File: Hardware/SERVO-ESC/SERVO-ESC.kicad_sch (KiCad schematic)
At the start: 43 parts, among them IC1 DRV8876PWPR, IC2 TMP102xxDRL, IC3 INA236AIDDFR, IC4 MT6816CT, IC5 AP2112K, J1 Conn_01x04_Pin, J2 Conn_01x04_Pin, J3 Conn_01x05_Pin, J4 Conn_01x05, J5 +, J6 -, U1 STM32F301C8Tx, Y1 25MHZ

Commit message: New PCB Files
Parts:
- removed C13: 100nF, Capacitor_SMD:C_0402_1005Metric, symbol Device:C
- removed C14, C16: 10nF, Capacitor_SMD:C_0402_1005Metric, symbol Device:C
- removed D1: 6V, Diode_SMD:D_0402_1005Metric, symbol Device:D
- removed FB1: 120, Inductor_SMD:L_0603_1608Metric, symbol Device:FerriteBead
- removed IC4: MT6816CT, Package_SO:SO-8_3.9x4.9mm_P1.27mm, symbol Sensor_Magnetic:MT6816CT
- removed J3: Conn_01x05_Pin, Connector_JST:JST_SH_SM05B-SRSS-TB_1x05-1MP_P1.00mm_Horizontal, symbol Connector:Conn_01x05_Pin
- added D1: LED, LED_SMD:LED_0603_1608Metric, symbol Device:LED
- added R1: 10k, Resistor_SMD:R_0402_1005Metric, symbol Device:R
- added R12, R13: 4.7k, Resistor_SMD:R_0402_1005Metric, symbol Device:R
- added R7: 1k, Resistor_SMD:R_0402_1005Metric, symbol Device:R
- J4: footprint Connector_PinSocket_1.00mm:PinSocket_1x05_P1.00mm_Vertical -> Connector_PinHeader_2.00mm:PinHeader_1x05_P2.00mm_Vertical
- renumbered C7 to C1, C3 to C10, C4 to C11, C15 to C12, C5 to C13, C6 to C14, C12 to C15, C8 to C2, C9 to C3, C10 to C4, C11 to C5, C17 to C6, C1 to C7, C18 to C8, C2 to C9, IC5 to IC1, IC1 to IC2, IC2 to IC4, IC3 to IC5, R2 to R10, R1 to R11, R7 to R2, R6 to R3, R5 to R4, R8 to R5, R9 to R6, R3 to R8, R4 to R9
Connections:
- net +3.3VA is gone; now on net +3.3V: C12.1, U1.9 (VDDA)
- net 3.3V is gone; now on net +3.3V: J2.4 (Pin_4)
- net +3.3V: now also D1.2 (A), R12.1, R13.1
- net GND: now also R1.1, R7.2
- net I2C-SCL-1: now also R5.2; no longer R6.2
- net I2C-SDA-1: now also R6.2, U1.43 (PB7); no longer R5.2, U1.41 (PB5)
- net INA236-INT: now also U1.45 (PB8), R12.2
- net MAG-MOSI: now also U1.28 (PB15); no longer U1.26 (PB13)
- net MAG-SCLK: now also U1.26 (PB13); no longer U1.28 (PB15)
- net TMP102-INT: now also R13.2
- net at U1.44 (BOOT0): now also R1.2
- net I2C-SCL-2 renamed UART-TX
- net I2C-SDA-2 renamed UART-RX
- new net: D1.1 (K), R7.1
- no-connect marks 2 -> 16
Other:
- moved on the sheet: C12, J4

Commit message: New Commit
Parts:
- removed J4: Conn_01x05, Connector_PinHeader_2.00mm:PinHeader_1x05_P2.00mm_Vertical, symbol Connector_Generic:Conn_01x05
- added C16: 10nF, Capacitor_SMD:C_0402_1005Metric, symbol Device:C
- added D2: TVS 6V, Diode_SMD:D_0402_1005Metric, symbol Diode:SMF6V0A
- added J3: MAG, Connector_PinSocket_2.00mm:PinSocket_1x04_P2.00mm_Vertical, symbol Connector:Conn_01x04_Pin
- added J4: Conn_01x04_Pin, Connector_PinSocket_2.54mm:PinSocket_1x04_P2.54mm_Vertical, symbol Connector:Conn_01x04_Pin
- added R14, R15: 4.7k, Resistor_SMD:R_0402_1005Metric, symbol Device:R
- added U2: MT6701CT, Package_SO:SO-8_3.9x4.9mm_P1.27mm, symbol Sensor_Magnetic:MT6701CT
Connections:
- net MAG-MISO is gone; now on net HBRIDGE-IN2: U1.27 (PB14)
- net MAG-MOSI is gone; now on net HBRIDGE-IN1: U1.28 (PB15)
- net +3.3V: now also R8.2, C16.1, D2.1 (A1), J3.4 (Pin_4), J4.4 (Pin_4), R14.1, R15.1, U2.1 (VDD), U2.2 (MODE), U2.8 (Z)
- net GND: now also C16.2, D2.2 (A2), J3.1 (Pin_1), J4.3 (Pin_3), U2.4 (GND); no longer R8.2
- net HBRIDGE-IN1: no longer U1.32 (PA11)
- net HBRIDGE-IN2: no longer U1.29 (PA8)
- net I2C-SDA-3: now reaches U1.41 (PB5)
- net I2C-SDA-3: now also J3.3 (Pin_3), J4.1 (Pin_1), R15.2, U2.6 (A)
- net MAG-SCLK: no longer names the net of U1.26 (PB13)
- new net I2C-SCL-3: J3.2 (Pin_2), J4.2 (Pin_2), R14.2, U1.29 (PA8), U2.7 (B)
- no-connect marks 16 -> 19
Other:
- moved on the sheet: C12, C15, R5, R6, R8

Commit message: New stuff
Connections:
- net +3.3V: no longer U1.9 (VDDA)
- new net +3.3VA: U1.9 (VDDA)
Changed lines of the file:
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@@
 	)
 	(junction
-		(at 57.15 21.59)
-		(diameter 0)
-		(color 0 0 0 0)
-	)
-	(junction
 		(at 60.96 135.89)
 		(diameter 0)
@@
 	(wire
 		(pts
-			(xy 57.15 21.59) (xy 59.69 21.59)
-		)
-		(stroke
-			(width 0)
-			(type default)
-		)
-	)
-	(wire
-		(pts
 			(xy 49.53 21.59) (xy 52.07 21.59)
 		)
@@
 					(unit 1)
 				)
+			)
+		)
+	)
+	(symbol
+		(lib_id "power:+3.3V")
+		(at 59.69 21.59 0)
+		(unit 1)
+		(exclude_from_sim no)
+		(in_bom yes)
+		(on_board yes)
+		(dnp no)
+		(fields_autoplaced yes)
+		(property "Reference" "#PWR054"
+			(at 59.69 25.4 0)
+			(effects
+				(font
+					(size 1.27 1.27)
+				)
+				(hide yes)
+			)
+		)
+		(property "Value" "+3.3VA"
+			(at 59.69 16.51 0)
+			(effects
+				(font
+					(size 1.27 1.27)
+				)
+			)
+		)
+		(property "Footprint" ""
+			(at 59.69 21.59 0)
+			(effects
+				(font
+					(size 1.27 1.27)
+				)
+				(hide yes)
+			)
+		)
+		(property "Datasheet" ""
+			(at 59.69 21.59 0)
+			(effects
+				(font
+					(size 1.27 1.27)
+				)
+				(hide yes)
+			)
+		)
+		(property "Description" "Power symbol creates a global label with name \"+3.3V\""
+			(at 59.69 21.59 0)
+			(effects
+				(font
+					(size 1.27 1.27)
+				)
+				(hide yes)
+			)
+		)
+		(pin "1"
+		)
+		(instances
+			(project "SERVO-ESC"
+				(path "/67d9952a-3813-4173-9c26-155df027e538"
+					(reference "#PWR054")
+					(unit 1)
+				)

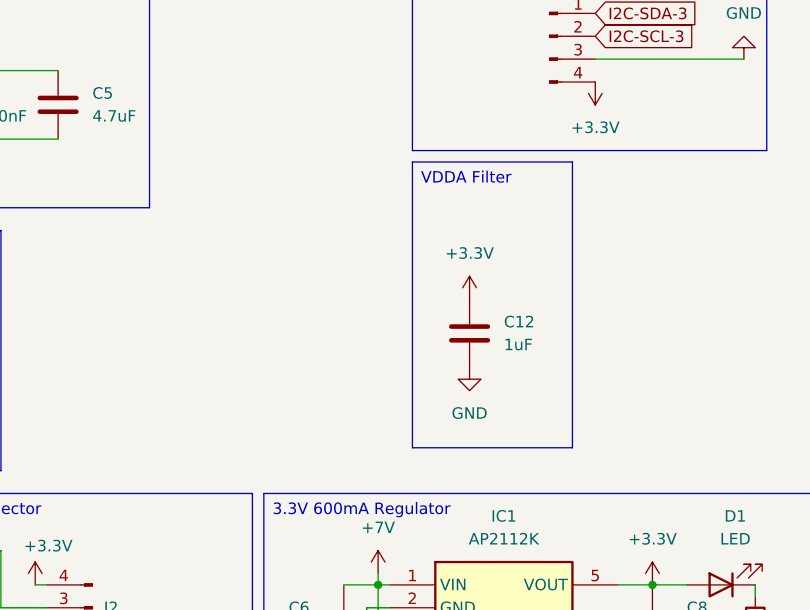
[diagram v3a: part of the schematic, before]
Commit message: New board files (messed up gnd via)
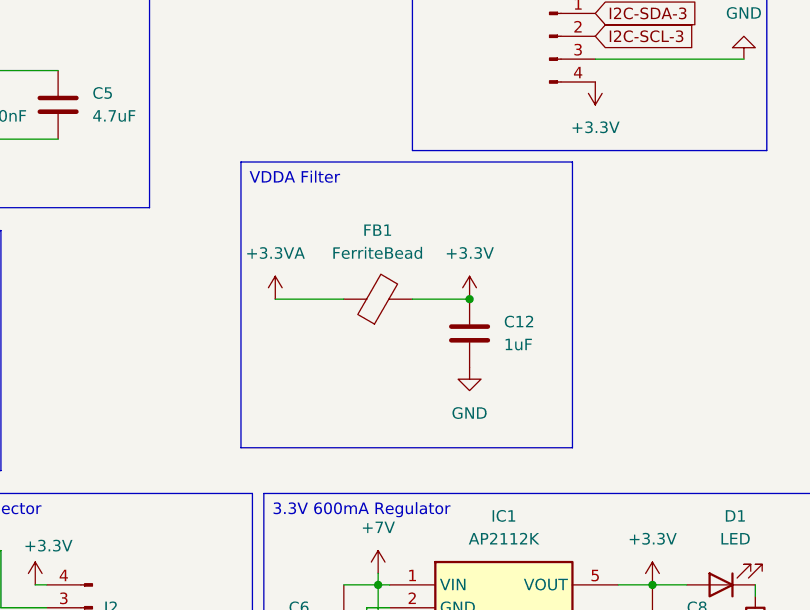
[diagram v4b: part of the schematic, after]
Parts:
- added FB1: FerriteBead, Inductor_SMD:L_0603_1608Metric, symbol Device:FerriteBead
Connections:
- net +3.3V: now also FB1.2
- net +3.3VA: now also FB1.1
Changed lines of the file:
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@@
 	(text_box "VDDA Filter\n"
 		(exclude_from_sim no)
-		(at 113.03 138.43 0)
-		(size 17.78 31.75)
+		(at 93.98 138.43 0)
+		(size 36.83 31.75)
 		(margins 0.9525 0.9525 0.9525 0.9525)
 		(stroke
@@
 	)
 	(junction
+		(at 119.38 153.67)
+		(diameter 0)
+		(color 0 0 0 0)
+	)
+	(junction
 		(at 220.98 76.2)
 		(diameter 0)
@@
 	(wire
 		(pts
+			(xy 97.79 153.67) (xy 105.41 153.67)
+		)
+		(stroke
+			(width 0)
+			(type default)
+		)
+	)
+	(wire
+		(pts
 			(xy 187.96 127) (xy 187.96 129.54)
 		)
@@
 	(wire
 		(pts
+			(xy 113.03 153.67) (xy 119.38 153.67)
+		)
+		(stroke
+			(width 0)
+			(type default)
+		)
+	)
+	(wire
+		(pts
 			(xy 110.49 190.5) (xy 109.22 190.5)
 		)
@@
 	)
 	(symbol
+		(lib_id "power:+3.3V")
+		(at 97.79 153.67 0)
+		(unit 1)
+		(exclude_from_sim no)
+		(in_bom yes)
+		(on_board yes)
+		(dnp no)
+		(fields_autoplaced yes)
+		(property "Reference" "#PWR055"
+			(at 97.79 157.48 0)
+			(effects
+				(font
+					(size 1.27 1.27)
+				)
+				(hide yes)
+			)
+		)
+		(property "Value" "+3.3VA"
+			(at 97.79 148.59 0)
+			(effects
+				(font
+					(size 1.27 1.27)
+				)
+			)
+		)
+		(property "Footprint" ""
+			(at 97.79 153.67 0)
+			(effects
+				(font
+					(size 1.27 1.27)
+				)
+				(hide yes)
+			)
+		)
+		(property "Datasheet" ""
+			(at 97.79 153.67 0)
+			(effects
+				(font
+					(size 1.27 1.27)
+				)
+				(hide yes)
+			)
+		)
+		(property "Description" "Power symbol creates a global label with name \"+3.3V\""
+			(at 97.79 153.67 0)
+			(effects
+				(font
+					(size 1.27 1.27)
+				)
+				(hide yes)
+			)
+		)
+		(pin "1"
+		)
+		(instances
+			(project "SERVO-ESC"
+				(path "/67d9952a-3813-4173-9c26-155df027e538"
+					(reference "#PWR055")
+					(unit 1)
+				)
+			)
+		)
+	)
+	(symbol
 		(lib_id "power:GND")
 		(at 232.41 165.1 0)
@@
 					(unit 1)
 				)
+			)
+		)
+	)
+	(symbol
+		(lib_id "Device:FerriteBead")
+		(at 109.22 153.67 90)
+		(unit 1)
+		(exclude_from_sim no)
+		(in_bom yes)
+		(on_board yes)
+		(dnp no)
+		(fields_autoplaced yes)
+		(property "Reference" "FB1"
+			(at 109.1692 146.05 90)
+			(effects
+				(font
+					(size 1.27 1.27)
+				)
+			)
+		)
+		(property "Value" "FerriteBead"
+			(at 109.1692 148.59 90)
+			(effects
+				(font
+					(size 1.27 1.27)
+				)
+			)
+		)
+		(property "Footprint" "Inductor_SMD:L_0603_1608Metric"
+			(at 109.22 155.448 90)
+			(effects
+				(font
+					(size 1.27 1.27)
+				)
+				(hide yes)
+			)
+		)
+		(property "Datasheet" "~"
+			(at 109.22 153.67 0)
+			(effects
+				(font
+					(size 1.27 1.27)
+				)
+				(hide yes)
+			)
+		)
+		(property "Description" "Ferrite bead"
+			(at 109.22 153.67 0)
+			(effects
+				(font
+					(size 1.27 1.27)
+				)
+				(hide yes)
+			)
+		)
+		(pin "1"
+		)
+		(pin "2"
+		)
+		(instances
+			(project ""
+				(path "/67d9952a-3813-4173-9c26-155df027e538"
+					(reference "FB1")
+					(unit 1)
+				)
